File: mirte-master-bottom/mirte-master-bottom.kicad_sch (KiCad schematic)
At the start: 5 parts, among them J17 Conn_01x03_Pin

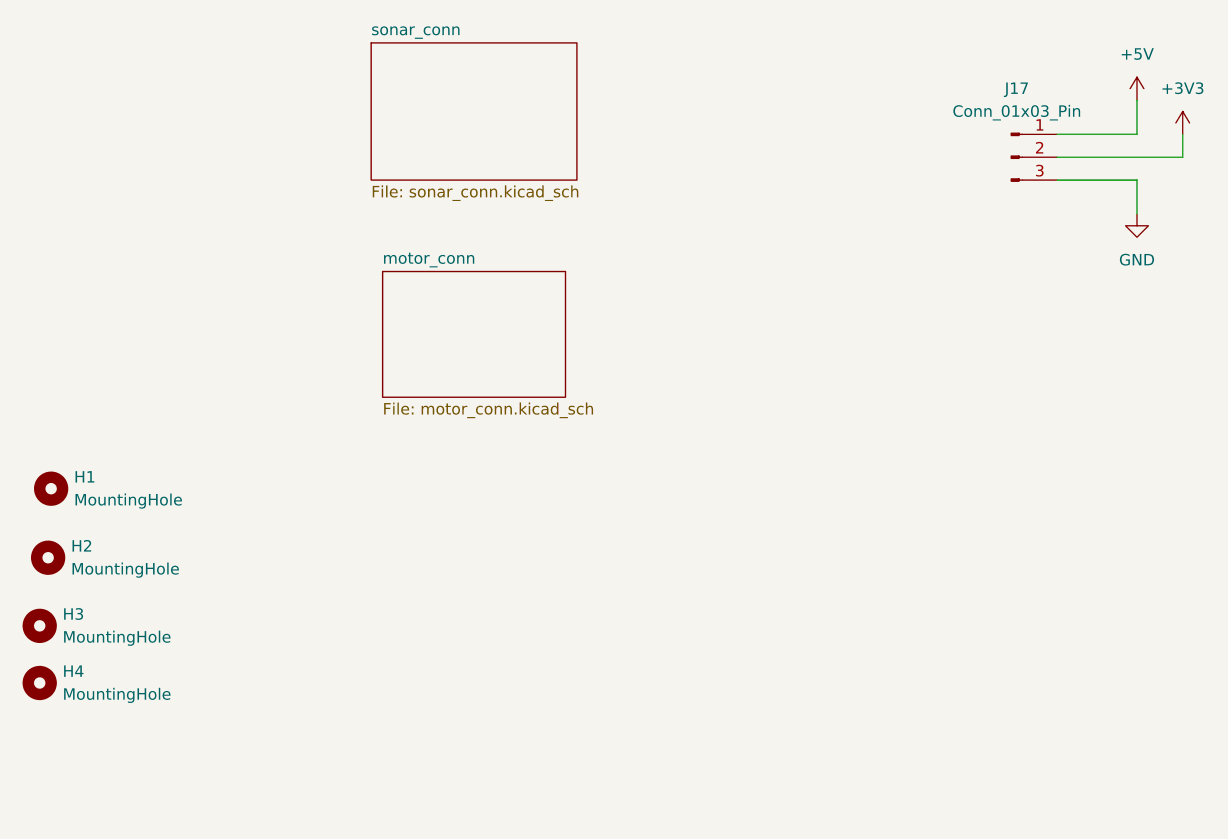
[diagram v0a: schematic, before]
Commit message: add usb switcher + finalize mirte-master
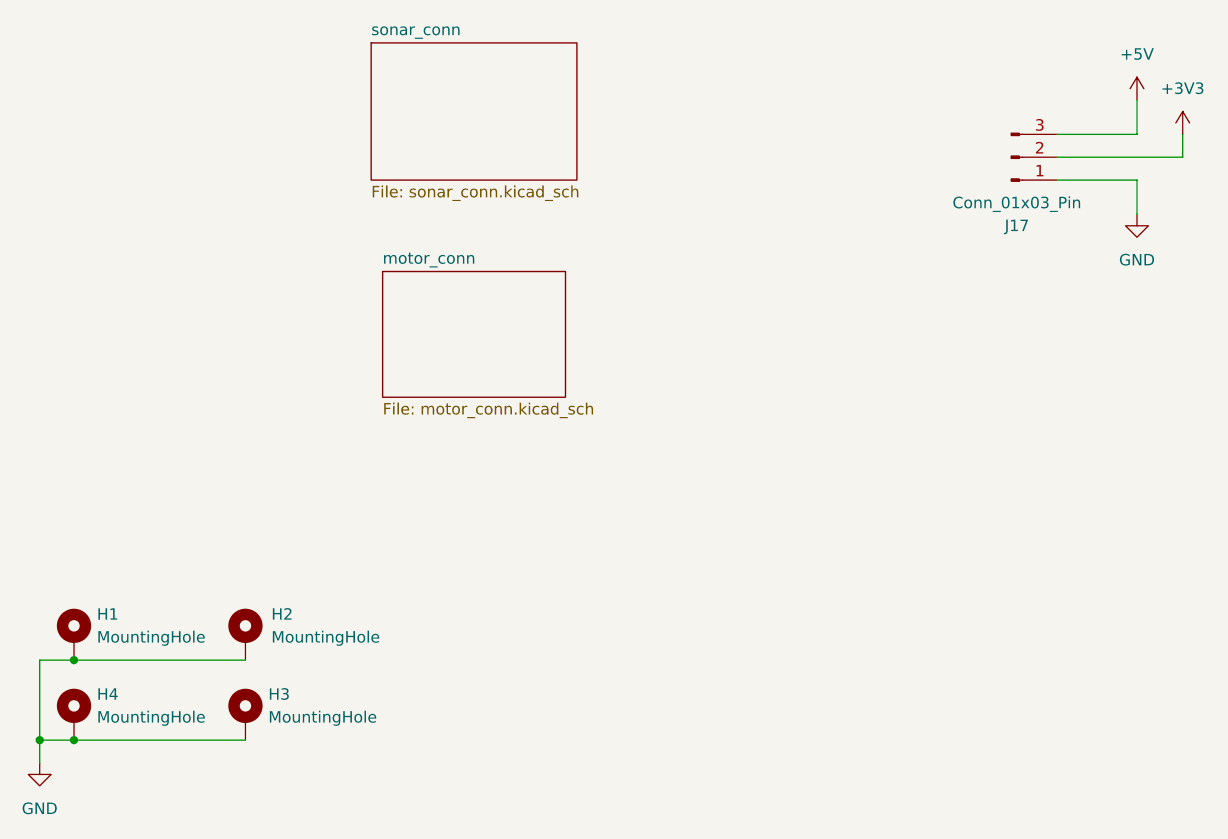
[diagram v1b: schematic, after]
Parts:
- H1, H2, H3, H4: footprint MountingHole:MountingHole_3.2mm_M3 -> MountingHole:MountingHole_3.2mm_M3_DIN965_Pad; symbol Mechanical:MountingHole -> Mechanical:MountingHole_Pad
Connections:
- net +5V: now also J17.3 (Pin_3); no longer J17.1 (Pin_1)
- net GND: now also H1.1, H2.1, H3.1, H4.1, J17.1 (Pin_1); no longer J17.3 (Pin_3)
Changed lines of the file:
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@@
 (kicad_sch (version 20230121) (generator eeschema)
   (paper "A4")
+  (junction (at 71.12 137.16) (diameter 0) (color 0 0 0 0)
+  )
+  (junction (at 71.12 146.05) (diameter 0) (color 0 0 0 0)
+  )
+  (junction (at 67.31 146.05) (diameter 0) (color 0 0 0 0)
+  )
+  (wire (pts (xy 67.31 146.05) (xy 71.12 146.05))
+    (stroke (width 0) (type default))
+  )
   (wire (pts (xy 189.23 87.63) (xy 189.23 83.82))
     (stroke (width 0) (type default))
   )
+  (wire (pts (xy 71.12 137.16) (xy 90.17 137.16))
+    (stroke (width 0) (type default))
+  )
   (wire (pts (xy 189.23 83.82) (xy 180.34 83.82))
     (stroke (width 0) (type default))
   )
+  (wire (pts (xy 67.31 137.16) (xy 71.12 137.16))
+    (stroke (width 0) (type default))
+  )
   (wire (pts (xy 194.31 78.74) (xy 194.31 81.28))
     (stroke (width 0) (type default))
@@
     (stroke (width 0) (type default))
   )
+  (wire (pts (xy 67.31 148.59) (xy 67.31 146.05))
+    (stroke (width 0) (type default))
+  )
+  (wire (pts (xy 67.31 146.05) (xy 67.31 137.16))
+    (stroke (width 0) (type default))
+  )
   (wire (pts (xy 189.23 74.93) (xy 189.23 78.74))
     (stroke (width 0) (type default))
   )
+  (wire (pts (xy 71.12 146.05) (xy 90.17 146.05))
+    (stroke (width 0) (type default))
+  )
   (wire (pts (xy 194.31 81.28) (xy 180.34 81.28))
     (stroke (width 0) (type default))
   )
-  (symbol (lib_id "Mechanical:MountingHole") (at 68.58 118.11 0) (unit 1)
-    (in_bom yes) (on_board yes) (dnp no) (fields_autoplaced)
-    (property "Reference" "H1" (at 71.12 116.84 0)
-      (effects (font (size 1.27 1.27)) (justify left))
-    )
-    (property "Value" "MountingHole" (at 71.12 119.38 0)
-      (effects (font (size 1.27 1.27)) (justify left))
-    )
-    (property "Footprint" "MountingHole:MountingHole_3.2mm_M3" (at 68.58 118.11 0)
-      (effects (font (size 1.27 1.27)) hide)
-    )
-    (property "Datasheet" "~" (at 68.58 118.11 0)
-      (effects (font (size 1.27 1.27)) hide)
-    )
+  (symbol (lib_id "Mechanical:MountingHole_Pad") (at 71.12 134.62 0) (unit 1)
+    (in_bom yes) (on_board yes) (dnp no) (fields_autoplaced)
+    (property "Reference" "H1" (at 73.66 132.08 0)
+      (effects (font (size 1.27 1.27)) (justify left))
+    )
+    (property "Value" "MountingHole" (at 73.66 134.62 0)
+      (effects (font (size 1.27 1.27)) (justify left))
+    )
+    (property "Footprint" "MountingHole:MountingHole_3.2mm_M3_DIN965_Pad" (at 71.12 134.62 0)
+      (effects (font (size 1.27 1.27)) hide)
+    )
+    (property "Datasheet" "~" (at 71.12 134.62 0)
+      (effects (font (size 1.27 1.27)) hide)
+    )
+    (pin "1")
     (instances
       (project "mirte-master-bottom"
@@
     )
   )
-  (symbol (lib_id "Mechanical:MountingHole") (at 67.31 139.7 0) (unit 1)
-    (in_bom yes) (on_board yes) (dnp no) (fields_autoplaced)
-    (property "Reference" "H4" (at 69.85 138.43 0)
-      (effects (font (size 1.27 1.27)) (justify left))
-    )
-    (property "Value" "MountingHole" (at 69.85 140.97 0)
-      (effects (font (size 1.27 1.27)) (justify left))
-    )
-    (property "Footprint" "MountingHole:MountingHole_3.2mm_M3" (at 67.31 139.7 0)
-      (effects (font (size 1.27 1.27)) hide)
-    )
-    (property "Datasheet" "~" (at 67.31 139.7 0)
-      (effects (font (size 1.27 1.27)) hide)
-    )
+  (symbol (lib_id "Mechanical:MountingHole_Pad") (at 71.12 143.51 0) (unit 1)
+    (in_bom yes) (on_board yes) (dnp no) (fields_autoplaced)
+    (property "Reference" "H4" (at 73.66 140.97 0)
+      (effects (font (size 1.27 1.27)) (justify left))
+    )
+    (property "Value" "MountingHole" (at 73.66 143.51 0)
+      (effects (font (size 1.27 1.27)) (justify left))
+    )
+    (property "Footprint" "MountingHole:MountingHole_3.2mm_M3_DIN965_Pad" (at 71.12 143.51 0)
+      (effects (font (size 1.27 1.27)) hide)
+    )
+    (property "Datasheet" "~" (at 71.12 143.51 0)
+      (effects (font (size 1.27 1.27)) hide)
+    )
+    (pin "1")
     (instances
       (project "mirte-master-bottom"
@@
     )
   )
-  (symbol (lib_id "Connector:Conn_01x03_Pin") (at 175.26 81.28 0) (unit 1)
-    (in_bom yes) (on_board yes) (dnp no) (fields_autoplaced)
-    (property "Reference" "J17" (at 175.895 73.66 0)
-      (effects (font (size 1.27 1.27)))
-    )
-    (property "Value" "Conn_01x03_Pin" (at 175.895 76.2 0)
+  (symbol (lib_id "Connector:Conn_01x03_Pin") (at 175.26 81.28 0) (mirror x) (unit 1)
+    (in_bom yes) (on_board yes) (dnp no)
+    (property "Reference" "J17" (at 175.895 88.9 0)
+      (effects (font (size 1.27 1.27)))
+    )
+    (property "Value" "Conn_01x03_Pin" (at 175.895 86.36 0)
       (effects (font (size 1.27 1.27)))
     )
@@
       (effects (font (size 1.27 1.27)) hide)
     )
-    (property "LCSC" "C144394" (at 175.895 73.66 0)
+    (property "LCSC" "C144394" (at 175.895 88.9 0)
       (effects (font (size 1.27 1.27)) hide)
     )
@@
     )
   )
-  (symbol (lib_id "Mechanical:MountingHole") (at 68.2452 125.7824 0) (unit 1)
-    (in_bom yes) (on_board yes) (dnp no) (fields_autoplaced)
-    (property "Reference" "H2" (at 70.7852 124.5124 0)
-      (effects (font (size 1.27 1.27)) (justify left))
-    )
-    (property "Value" "MountingHole" (at 70.7852 127.0524 0)
-      (effects (font (size 1.27 1.27)) (justify left))
-    )
-    (property "Footprint" "MountingHole:MountingHole_3.2mm_M3" (at 68.2452 125.7824 0)
-      (effects (font (size 1.27 1.27)) hide)
-    )
-    (property "Datasheet" "~" (at 68.2452 125.7824 0)
-      (effects (font (size 1.27 1.27)) hide)
-    )
+  (symbol (lib_id "Mechanical:MountingHole_Pad") (at 90.17 134.62 0) (unit 1)
+    (in_bom yes) (on_board yes) (dnp no) (fields_autoplaced)
+    (property "Reference" "H2" (at 93.0448 132.08 0)
+      (effects (font (size 1.27 1.27)) (justify left))
+    )
+    (property "Value" "MountingHole" (at 93.0448 134.62 0)
+      (effects (font (size 1.27 1.27)) (justify left))
+    )
+    (property "Footprint" "MountingHole:MountingHole_3.2mm_M3_DIN965_Pad" (at 90.17 134.62 0)
+      (effects (font (size 1.27 1.27)) hide)
+    )
+    (property "Datasheet" "~" (at 90.17 134.62 0)
+      (effects (font (size 1.27 1.27)) hide)
+    )
+    (pin "1")
     (instances
       (project "mirte-master-bottom"
@@
     )
   )
-  (symbol (lib_id "Mechanical:MountingHole") (at 67.31 133.35 0) (unit 1)
-    (in_bom yes) (on_board yes) (dnp no) (fields_autoplaced)
-    (property "Reference" "H3" (at 69.85 132.08 0)
-      (effects (font (size 1.27 1.27)) (justify left))
-    )
-    (property "Value" "MountingHole" (at 69.85 134.62 0)
-      (effects (font (size 1.27 1.27)) (justify left))
-    )
-    (property "Footprint" "MountingHole:MountingHole_3.2mm_M3" (at 67.31 133.35 0)
-      (effects (font (size 1.27 1.27)) hide)
-    )
-    (property "Datasheet" "~" (at 67.31 133.35 0)
-      (effects (font (size 1.27 1.27)) hide)
-    )
-    (instances
-      (project "mirte-master-bottom"
+  (symbol (lib_id "power:GND") (at 67.31 148.59 0) (unit 1)
+    (in_bom yes) (on_board yes) (dnp no) (fields_autoplaced)
+    (property "Reference" "#PWR024" (at 67.31 154.94 0)
+      (effects (font (size 1.27 1.27)) hide)
+    )
+    (property "Value" "GND" (at 67.31 153.67 0)
+      (effects (font (size 1.27 1.27)))
+    )
+    (property "Footprint" "" (at 67.31 148.59 0)
+      (effects (font (size 1.27 1.27)) hide)
+    )
+    (property "Datasheet" "" (at 67.31 148.59 0)
+      (effects (font (size 1.27 1.27)) hide)
+    )
+    (pin "1")
+    (instances
+      (project "mirte-master-bottom"
+        (path "/c479422a-501d-4123-8665-56a1c70bd9ea"
+          (reference "#PWR024") (unit 1)
+        )
+      )
+    )
+  )
+  (symbol (lib_id "Mechanical:MountingHole_Pad") (at 90.17 143.51 0) (unit 1)
+    (in_bom yes) (on_board yes) (dnp no) (fields_autoplaced)
+    (property "Reference" "H3" (at 92.71 140.97 0)
+      (effects (font (size 1.27 1.27)) (justify left))
+    )
+    (property "Value" "MountingHole" (at 92.71 143.51 0)
+      (effects (font (size 1.27 1.27)) (justify left))
+    )
+    (property "Footprint" "MountingHole:MountingHole_3.2mm_M3_DIN965_Pad" (at 90.17 143.51 0)
+      (effects (font (size 1.27 1.27)) hide)
+    )
+    (property "Datasheet" "~" (at 90.17 143.51 0)
+      (effects (font (size 1.27 1.27)) hide)
+    )
+    (pin "1")
+    (instances
+      (project "mirte-master-bottom"

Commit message: add some interesting parts
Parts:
- added J4, J9: Conn_01x20_Socket, Connector_PinHeader_2.54mm:PinHeader_1x20_P2.54mm_Vertical, symbol Connector:Conn_01x20_Socket
- added K1: SANYOU_SRD_Form_A, Relay_THT:Relay_SPST_SANYOU_SRD_Series_Form_A, symbol Relay:SANYOU_SRD_Form_A
- added U1: PCA9685PW, Package_SO:TSSOP-28_4.4x9.7mm_P0.65mm, symbol Driver_LED:PCA9685PW
- added U2: INA226, Package_SO:VSSOP-10_3x3mm_P0.5mm, symbol Sensor_Energy:INA226
- added U3, U4: DRV8871DDA, Package_SO:Texas_HTSOP-8-1EP_3.9x4.9mm_P1.27mm_EP2.95x4.9mm_Mask2.4x3.1mm_ThermalVias, symbol Driver_Motor:DRV8871DDA
- added U5: TPS82130, Package_LGA:Texas_SIL0008D_MicroSiP-8-1EP_2.8x3mm_P0.65mm_EP1.1x1.9mm_ThermalVias, symbol Regulator_Switching:TPS82130
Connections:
- new net: U4.1 (GND), U4.7 (GND), U4.9 (GND)
- new net: U3.1 (GND), U3.7 (GND), U3.9 (GND)
- new net: U5.3 (GND), U5.9 (GND)
- new net: U5.4 (VOUT), U5.5 (VOUT)

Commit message: first schematic and layout bottom pcb v3
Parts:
- removed U1: PCA9685PW, Package_SO:TSSOP-28_4.4x9.7mm_P0.65mm, symbol Driver_LED:PCA9685PW
- removed U2: INA226, Package_SO:VSSOP-10_3x3mm_P0.5mm, symbol Sensor_Energy:INA226
- removed U3, U4: DRV8871DDA, Package_SO:Texas_HTSOP-8-1EP_3.9x4.9mm_P1.27mm_EP2.95x4.9mm_Mask2.4x3.1mm_ThermalVias, symbol Driver_Motor:DRV8871DDA
- removed U5: TPS82130, Package_LGA:Texas_SIL0008D_MicroSiP-8-1EP_2.8x3mm_P0.65mm_EP1.1x1.9mm_ThermalVias, symbol Regulator_Switching:TPS82130
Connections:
- net +3V3: now also J4.5 (Pin_5)
- net +5V: now also J4.2 (Pin_2)
- net GND: now also J4.3 (Pin_3)
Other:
- added sheet power (power.kicad_sch)
- sheet sonar_conn ports: added SONARS; removed none

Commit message: verder v3 pcb
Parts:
- removed J17: Conn_01x03_Pin, Connector_JST:JST_XH_B3B-XH-A_1x03_P2.50mm_Vertical, symbol Connector:Conn_01x03_Pin
- removed J4, J9: Conn_01x20_Socket, Connector_PinHeader_2.54mm:PinHeader_1x20_P2.54mm_Vertical, symbol Connector:Conn_01x20_Socket
- removed K1: SANYOU_SRD_Form_A, Relay_THT:Relay_SPST_SANYOU_SRD_Series_Form_A, symbol Relay:SANYOU_SRD_Form_A
- added A1: RaspberryPi-PicoH, Module:RaspberryPi_Pico_Common_THT, symbol custom:RaspberryPi-Pico-H
- added J13: oled_conn, Connector_JST:JST_XH_B4B-XH-A_1x04_P2.50mm_Vertical, symbol Connector:Conn_01x04_Socket
- added Q1: DMG2305UX, Package_TO_SOT_SMD:SOT-23, symbol Transistor_FET:DMG2301L
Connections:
- net +3V3: now also A1.36 (3V3)
- net +5V: now also J13.2 (Pin_2), Q1.3 (D)
- net GND: now also A1.13 (GND), A1.18 (GND), A1.23 (GND), A1.28 (GND), A1.3 (GND), A1.33 (AGND), A1.38 (GND), A1.8 (GND), J13.1 (Pin_1)
- new net 1A: A1.14 (GPIO10)
- new net 1B: A1.15 (GPIO11)
- new net 2A: A1.16 (GPIO12)
- new net 2B: A1.17 (GPIO13)
- new net 3A: A1.4 (GPIO2)
- new net 3B: A1.5 (GPIO3)
- new net 4A: A1.34 (GPIO28_ADC2)
- new net 4B: A1.31 (GPIO26_ADC0)
- new net A1: A1.19 (GPIO14)
- new net A2: A1.21 (GPIO16)
- new net A3: A1.25 (GPIO19)
- new net A4: A1.26 (GPIO20)
- new net B1: A1.20 (GPIO15)
- new net B2: A1.22 (GPIO17)
- new net B3: A1.24 (GPIO18)
- new net B4: A1.27 (GPIO21)
- new net E0: A1.10 (GPIO7)
- new net E1: A1.12 (GPIO9)
- new net LED_STRIP: A1.29 (GPIO22)
- new net POWER_RELAY: A1.32 (GPIO27_ADC1)
- new net RX: A1.2 (GPIO1)
- new net SCL: A1.7 (GPIO5), J13.3 (Pin_3)
- new net SDA: A1.6 (GPIO4), J13.4 (Pin_4)
- new net T0: A1.9 (GPIO6)
- new net T1: A1.11 (GPIO8)
- new net TX: A1.1 (GPIO0)
- new net VBUS: A1.40 (VBUS), Q1.1 (G)
- new net VSYS: A1.39 (VSYS), Q1.2 (S)
- no-connect marks 0 -> 3
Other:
- added sheet uart_servos (uart_servos.kicad_sch)
- sheet motor_conn ports: added {ENCODER}, {PWMS}; removed none
- sheet power ports: added PWR_IN_SIG; removed none
- sheet sonar_conn ports: added {SONARS}; removed SONARS
- note added: "2"
- note added: "Connect VSYS to 5V if no USB is plugged into the rpi-pico"

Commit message: upd main layout v3
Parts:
- added R23, R31: 4k7, Resistor_SMD:R_0805_2012Metric, symbol Device:R
- A1: footprint Module:RaspberryPi_Pico_Common_THT -> raspberry_pi_pico:RaspberryPi_Pico_Common_THT
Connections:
- net +5V: now also R23.1, R31.1
- net SCL: now also R23.2
- net SDA: now also R31.2
- net LED_STRIP renamed PWR_IN_SIG
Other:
- sheet power ports: added RELAY_PWR; removed none
